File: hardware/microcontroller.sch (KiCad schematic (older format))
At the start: 35 parts, among them P2 USB_OTG, P3 ICSP, P4 STATUS 1, P5 STATUS 2, P6 UART, P7 JTAG, SW1 RESET, U4 ATMEGA32U4-AU, X2 16MHz

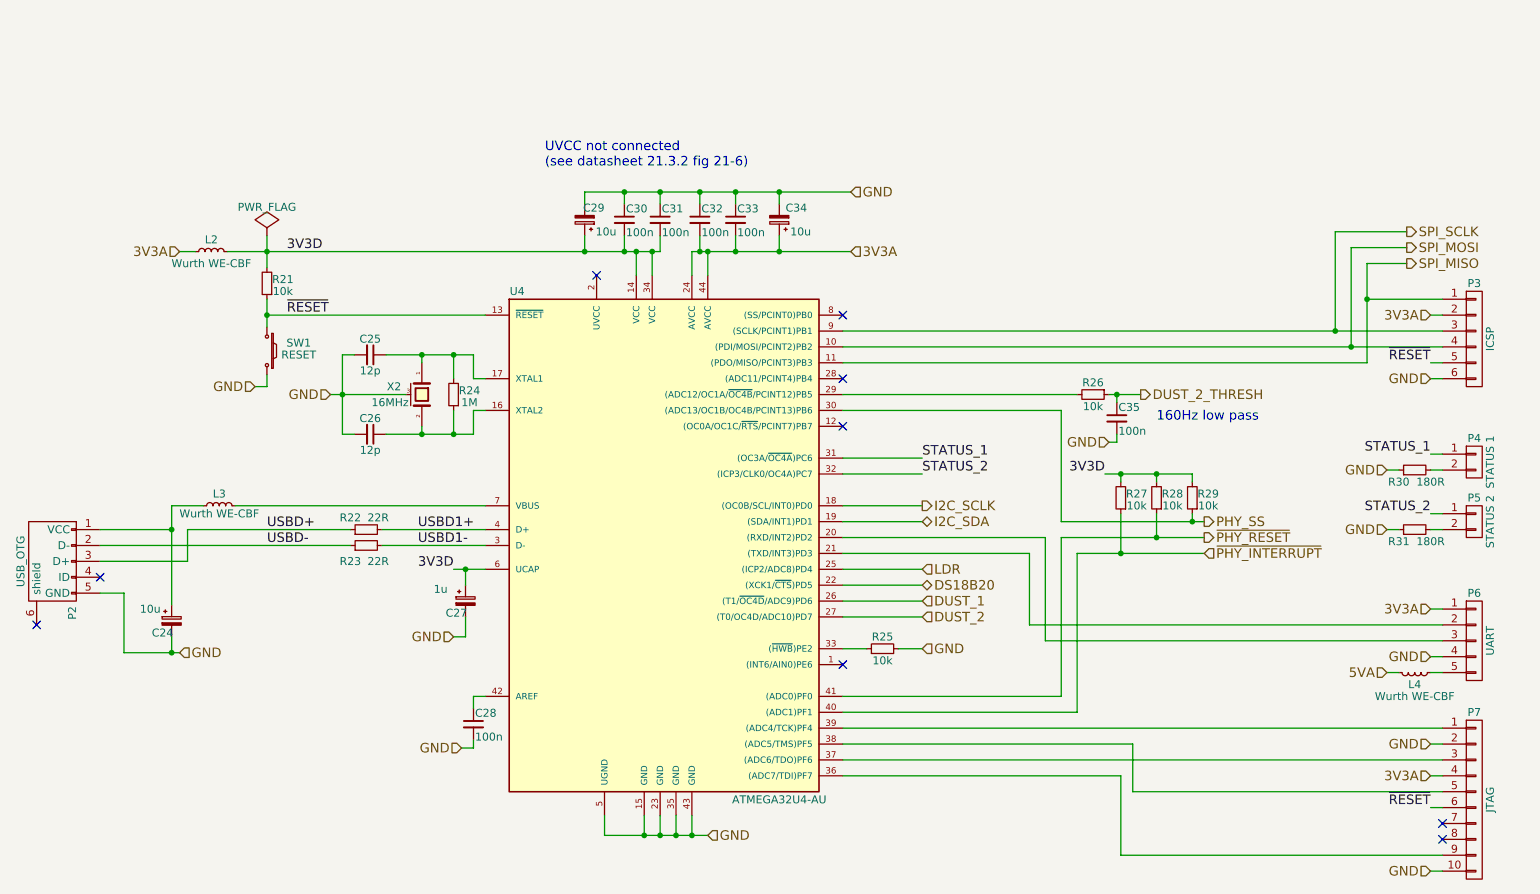
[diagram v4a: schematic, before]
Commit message: Added some part numbers to the schematic
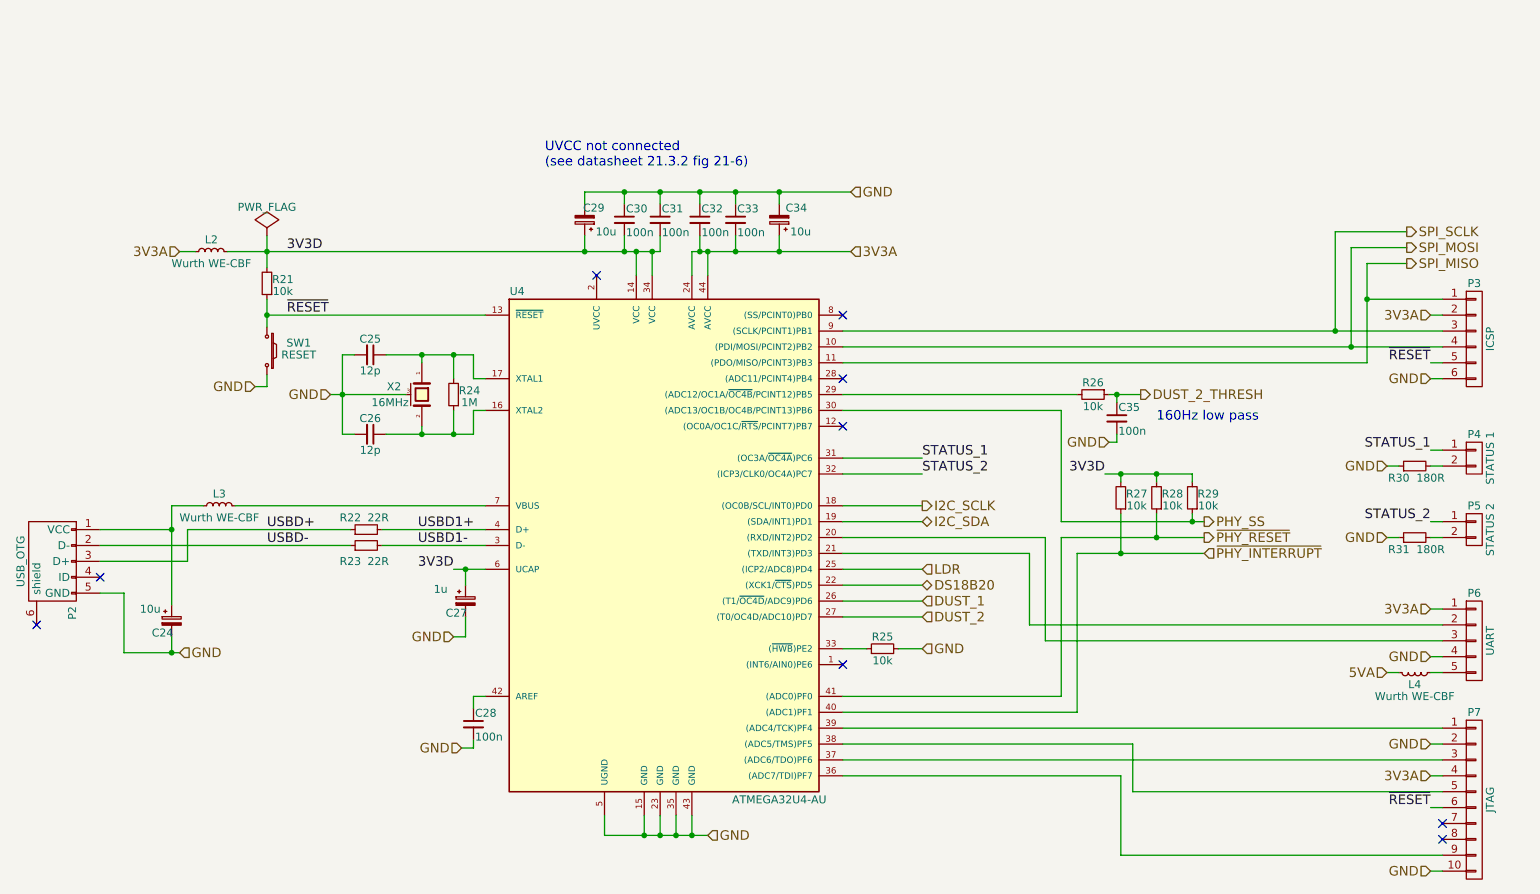
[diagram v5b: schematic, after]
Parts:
- L2, L3, L4: MPN1 (none) -> 7447918; Manufacturer1 (none) -> Wurth Elektronik; SKU1 (none) -> 124-1871; Vendor1 (none) -> RS
- P2: MPN1 (none) -> 10103594-0001LF; Manufacturer1 (none) -> Amphenol; SKU1 (none) -> 649-10103594-0001LF; Vendor1 (none) -> Mouser
- P4, P5: MPN1 (none) -> 22-27-2021; Manufacturer1 (none) -> Molex; SKU1 (none) -> 483-8461; Vendor1 (none) -> RS
- U4: MPN1 (none) -> ATMEGA32U4-AU; Manufacturer1 (none) -> Microchip Technology; SKU1 (none) -> 131-0289; Vendor1 (none) -> RS
- X2: MPN1 (none) -> Q22FA2380018111; Manufacturer1 (none) -> Epson; SKU1 (none) -> 667-6209; Vendor1 (none) -> RS
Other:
- moved on the sheet: P4, R30, R31
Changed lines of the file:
@@
 F 2 "Housings_QFP:TQFP-44_10x10mm_Pitch0.8mm" H 5275 3950 50  0001 C CIN
 F 3 "" H 6375 5050 50  0000 C CNN
+F 4 "Microchip Technology" H 5275 3950 60  0001 C CNN "Manufacturer1"
+F 5 "ATMEGA32U4-AU" H 5275 3950 60  0001 C CNN "MPN1"
+F 6 "RS" H 5275 3950 60  0001 C CNN "Vendor1"
+F 7 "131-0289" H 5275 3950 60  0001 C CNN "SKU1"
 	1    5275 3950
 	1    0    0    -1
@@
 F 2 "Crystals:crystal_FA238-TSX3225" H 3725 2900 50  0001 C CNN
 F 3 "" H 3725 2900 50  0000 C CNN
+F 4 "Epson" V 3725 2900 60  0001 C CNN "Manufacturer1"
+F 5 "Q22FA2380018111" V 3725 2900 60  0001 C CNN "MPN1"
+F 6 "RS" V 3725 2900 60  0001 C CNN "Vendor1"
+F 7 "667-6209" V 3725 2900 60  0001 C CNN "SKU1"
 	1    3725 2900
 	0    1    1    0
@@
 F 2 "Connect:USB_Micro-B_10103594-0001LF" V 1350 3850 50  0001 C CNN
 F 3 "" V 1350 3850 50  0000 C CNN
+F 4 "Amphenol" H 1400 3950 60  0001 C CNN "Manufacturer1"
+F 5 "10103594-0001LF" H 1400 3950 60  0001 C CNN "MPN1"
+F 6 "Mouser" H 1400 3950 60  0001 C CNN "Vendor1"
+F 7 "649-10103594-0001LF" H 1400 3950 60  0001 C CNN "SKU1"
 	1    1400 3950
 	0    -1   1    0
@@
 F 2 "Choke_SMD:Choke_SMD_1206_Standard" H 9975 4650 50  0001 C CNN
 F 3 "" H 9975 4650 50  0000 C CNN
+F 4 "Wurth Elektronik" V 9975 4650 60  0001 C CNN "Manufacturer1"
+F 5 "7447918" V 9975 4650 60  0001 C CNN "MPN1"
+F 6 "RS" V 9975 4650 60  0001 C CNN "Vendor1"
+F 7 "124-1871" V 9975 4650 60  0001 C CNN "SKU1"
 	1    9975 4650
 	0    1    1    0
@@
 $EndComp
 $Comp
-L L_Small L3
-U 1 1 59EF73D9
-P 2450 3600
-F 0 "L3" V 2525 3600 50  0000 C CNN
-F 1 "Wurth WE-CBF" V 2400 3600 50  0000 C CNN
-F 2 "Choke_SMD:Choke_SMD_1206_Standard" H 2450 3600 50  0001 C CNN
-F 3 "" H 2450 3600 50  0000 C CNN
-	1    2450 3600
-	0    -1   -1   0
-$EndComp
-$Comp
 L R_Small R30
 U 1 1 59EFC538
-P 9975 3375
-F 0 "R30" V 9900 3475 50  0000 C CNN
-F 1 "180R" V 9900 3275 50  0000 C CNN
-F 2 "Resistors_SMD:R_1206" H 9975 3375 50  0001 C CNN
-F 3 "" H 9975 3375 50  0000 C CNN
-	1    9975 3375
+P 9975 3350
+F 0 "R30" V 9900 3450 50  0000 C CNN
+F 1 "180R" V 9900 3250 50  0000 C CNN
+F 2 "Resistors_SMD:R_1206" H 9975 3350 50  0001 C CNN
+F 3 "" H 9975 3350 50  0000 C CNN
+	1    9975 3350
 	0    -1   -1   0
 $EndComp
@@
 F 2 "Choke_SMD:Choke_SMD_1206_Standard" H 2400 2000 50  0001 C CNN
 F 3 "" H 2400 2000 50  0000 C CNN
+F 4 "Wurth Elektronik" V 2400 2000 60  0001 C CNN "Manufacturer1"
+F 5 "7447918" V 2400 2000 60  0001 C CNN "MPN1"
+F 6 "RS" V 2400 2000 60  0001 C CNN "Vendor1"
+F 7 "124-1871" V 2400 2000 60  0001 C CNN "SKU1"
 	1    2400 2000
 	0    -1   -1   0
@@
 L CONN_01X02 P4
 U 1 1 59DC89D9
-P 10350 3325
-F 0 "P4" H 10350 3475 50  0000 C CNN
-F 1 "STATUS 1" V 10450 3325 50  0000 C CNN
-F 2 "Connectors_Molex:Molex_KK-6410-02_02x2.54mm_Straight" H 10350 3325 50  0001 C CNN
-F 3 "" H 10350 3325 50  0000 C CNN
-	1    10350 3325
-	1    0    0    -1
-$EndComp
-$Comp
-L CONN_01X02 P5
-U 1 1 59DCC0CC
-P 10350 3700
-F 0 "P5" H 10350 3850 50  0000 C CNN
-F 1 "STATUS 2" V 10450 3700 50  0000 C CNN
-F 2 "Connectors_Molex:Molex_KK-6410-02_02x2.54mm_Straight" H 10350 3700 50  0001 C CNN
-F 3 "" H 10350 3700 50  0000 C CNN
-	1    10350 3700
-	1    0    0    -1
-$EndComp
-Text HLabel 9800 3375 0    60   Input ~ 0
-GND
-Text HLabel 9800 3750 0    60   Input ~ 0
+P 10350 3300
+F 0 "P4" H 10350 3450 50  0000 C CNN
+F 1 "STATUS 1" V 10450 3300 50  0000 C CNN
+F 2 "Connectors_Molex:Molex_KK-6410-02_02x2.54mm_Straight" H 10350 3300 50  0001 C CNN
+F 3 "" H 10350 3300 50  0000 C CNN
+F 4 "Molex" H 10350 3300 60  0001 C CNN "Manufacturer1"
+F 5 "22-27-2021" H 10350 3300 60  0001 C CNN "MPN1"
+F 6 "RS" H 10350 3300 60  0001 C CNN "Vendor1"
+F 7 "483-8461" H 10350 3300 60  0001 C CNN "SKU1"
+	1    10350 3300
+	1    0    0    -1
+$EndComp
+Text HLabel 9800 3350 0    60   Input ~ 0
+GND
+Text HLabel 9800 3800 0    60   Input ~ 0
 GND
 $Comp
 L R_Small R31
 U 1 1 59DCE73D
-P 9975 3750
-F 0 "R31" V 9900 3850 50  0000 C CNN
-F 1 "180R" V 9900 3650 50  0000 C CNN
-F 2 "Resistors_SMD:R_1206" H 9975 3750 50  0001 C CNN
-F 3 "" H 9975 3750 50  0000 C CNN
-	1    9975 3750
+P 9975 3800
+F 0 "R31" V 9900 3900 50  0000 C CNN
+F 1 "180R" V 9900 3700 50  0000 C CNN
+F 2 "Resistors_SMD:R_1206" H 9975 3800 50  0001 C CNN
+F 3 "" H 9975 3800 50  0000 C CNN
+	1    9975 3800
 	0    -1   -1   0
 $EndComp
@@
 Text Label 6875 3400 0    60   ~ 0
 STATUS_2
-Text Label 10075 3275 2    60   ~ 0
+Text Label 10075 3250 2    60   ~ 0
 STATUS_1
-Text Label 10075 3650 2    60   ~ 0
+Text Label 10075 3700 2    60   ~ 0
 STATUS_2
 Text HLabel 6875 4100 2    60   BiDi ~ 0
@@
 	3225 3150 3300 3150
 Wire Wire Line
-	3225 2650 3225 3150
+	3225 2650 3225 2900
+Wire Wire Line
+	3225 2900 3225 3150
 Wire Wire Line
 	3225 2650 3300 2650
 Wire Wire Line
-	3150 2900 3625 2900
+	3150 2900 3225 2900
+Wire Wire Line
+	3225 2900 3625 2900
 Connection ~ 3225 2900
 Wire Wire Line
-	6375 2500 10150 2500
-Wire Wire Line
-	6375 2600 10150 2600
+	6375 2500 9475 2500
+Wire Wire Line
+	9475 2500 10150 2500
+Wire Wire Line
+	6375 2600 9575 2600
+Wire Wire Line
+	9575 2600 10150 2600
 Wire Wire Line
 	9675 2700 6375 2700
 Wire Wire Line
-	2750 2300 2750 2475
+	2750 2300 2750 2400
+Wire Wire Line
+	2750 2400 2750 2475
 Connection ~ 2750 2400
 Wire Wire Line
-	2750 1900 2750 2100
-Wire Wire Line
-	2500 2000 5225 2000
+	2750 1900 2750 2000
+Wire Wire Line
+	2750 2000 2750 2100
+Wire Wire Line
+	2500 2000 2750 2000
+Wire Wire Line
+	2750 2000 4750 2000
+Wire Wire Line
+	4750 2000 5000 2000
+Wire Wire Line
+	5000 2000 5075 2000
+Wire Wire Line
+	5075 2000 5175 2000
+Wire Wire Line
+	5175 2000 5225 2000
 Wire Wire Line
 	10150 2300 9675 2300
 Wire Wire Line
-	9675 2075 9675 2700
+	9675 2075 9675 2300
+Wire Wire Line
+	9675 2300 9675 2700
 Wire Wire Line
 	10075 2400 10150 2400
@@
 	8100 2950 8100 2900
 Wire Wire Line
-	8050 2900 8250 2900
+	8050 2900 8100 2900
+Wire Wire Line
+	8100 2900 8250 2900
 Connection ~ 8100 2900
 Wire Wire Line
@@
 Connection ~ 5075 2000
 Wire Wire Line
-	5425 2000 6425 2000
+	5425 2000 5475 2000
+Wire Wire Line
+	5475 2000 5525 2000
+Wire Wire Line
+	5525 2000 5700 2000
+Wire Wire Line
+	5700 2000 5975 2000
+Wire Wire Line
+	5975 2000 6425 2000
 Wire Wire Line
 	5525 2000 5525 2150
@@
 	4750 1625 4750 1700
 Wire Wire Line
-	4750 1625 6425 1625
+	4750 1625 5000 1625
+Wire Wire Line
+	5000 1625 5225 1625
+Wire Wire Line
+	5225 1625 5475 1625
+Wire Wire Line
+	5475 1625 5700 1625
+Wire Wire Line
+	5700 1625 5975 1625
+Wire Wire Line
+	5975 1625 6425 1625
 Wire Wire Line
 	5000 1625 5000 1700
@@
 Connection ~ 5975 1625
 Wire Wire Line
-	3500 2650 4050 2650
+	3500 2650 3725 2650
+Wire Wire Line
+	3725 2650 3925 2650
+Wire Wire Line
+	3925 2650 4050 2650
 Wire Wire Line
 	3725 2650 3725 2700
 Wire Wire Line
-	3500 3150 4050 3150
+	3500 3150 3725 3150
+Wire Wire Line
+	3725 3150 3925 3150
+Wire Wire Line
+	3925 3150 4050 3150
 Wire Wire Line
 	3725 3150 3725 3100
@@
 	4125 3600 2550 3600
 Wire Wire Line
-	4875 5675 5525 5675
-Wire Wire Line
-	3925 4000 4125 4000
+	4875 5675 5125 5675
+Wire Wire Line
+	5125 5675 5225 5675
+Wire Wire Line
+	5225 5675 5325 5675
+Wire Wire Line
+	5325 5675 5425 5675
+Wire Wire Line
+	5425 5675 5525 5675
+Wire Wire Line
+	3925 4000 4000 4000
+Wire Wire Line
+	4000 4000 4125 4000
 Wire Wire Line
 	4000 4000 4000 4100
@@
 	2350 3600 2150 3600
 Wire Wire Line
-	2150 3600 2150 4225
+	2150 3600 2150 3750
+Wire Wire Line
+	2150 3750 2150 4225
 Wire Wire Line
 	2150 3750 1700 3750
@@
 	1850 4150 1850 4525
 Wire Wire Line
-	1850 4525 2200 4525
+	1850 4525 2150 4525
+Wire Wire Line
+	2150 4525 2200 4525
 Wire Wire Line
 	2150 4525 2150 4425
@@
 	7750 3000 7750 3700
 Wire Wire Line
-	7750 3700 8650 3700
+	7750 3700 8575 3700
+Wire Wire Line
+	8575 3700 8650 3700
 Wire Wire Line
 	8575 3650 8575 3700
@@
 	8575 3400 8575 3450
 Wire Wire Line
-	8025 3400 8575 3400
+	8025 3400 8125 3400
+Wire Wire Line
+	8125 3400 8350 3400
+Wire Wire Line
+	8350 3400 8575 3400
 Wire Wire Line
 	8350 3650 8350 3800
 Wire Wire Line
-	7750 3800 8650 3800
+	7750 3800 8350 3800
+Wire Wire Line
+	8350 3800 8650 3800
 Wire Wire Line
 	8125 3650 8125 3900
 Wire Wire Line
-	7850 3900 8650 3900
+	7850 3900 8125 3900
+Wire Wire Line
+	8125 3900 8650 3900
 Wire Wire Line
 	8350 3450 8350 3400
@@
 	6375 3400 6875 3400
 Wire Wire Line
-	10150 3275 10075 3275
-Wire Wire Line
-	10150 3375 10075 3375
-Wire Wire Line
-	9875 3375 9800 3375
-Wire Wire Line
-	10150 3650 10075 3650
-Wire Wire Line
-	10075 3750 10150 3750
-Wire Wire Line
-	9875 3750 9800 3750
+	10150 3250 10075 3250
+Wire Wire Line
+	10150 3350 10075 3350
+Wire Wire Line
+	9875 3350 9800 3350
+Wire Wire Line
+	10150 3700 10075 3700
+Wire Wire Line
+	10075 3800 10150 3800
+Wire Wire Line
+	9875 3800 9800 3800
 Wire Wire Line
 	6375 4100 6875 4100
+$Comp
+L CONN_01X02 P5
+U 1 1 59DFF1F9
+P 10350 3750
+F 0 "P5" H 10350 3900 50  0000 C CNN
+F 1 "STATUS 2" V 10450 3750 50  0000 C CNN
+F 2 "Connectors_Molex:Molex_KK-6410-02_02x2.54mm_Straight" H 10350 3750 50  0001 C CNN
+F 3 "" H 10350 3750 50  0000 C CNN
+F 4 "Molex" H 10350 3750 60  0001 C CNN "Manufacturer1"
+F 5 "22-27-2021" H 10350 3750 60  0001 C CNN "MPN1"
+F 6 "RS" H 10350 3750 60  0001 C CNN "Vendor1"
+F 7 "483-8461" H 10350 3750 60  0001 C CNN "SKU1"
+	1    10350 3750
+	1    0    0    -1
+$EndComp
+$Comp
+L L_Small L3
+U 1 1 59E04F6E
+P 2450 3600
+F 0 "L3" V 2525 3600 50  0000 C CNN
+F 1 "Wurth WE-CBF" V 2375 3600 50  0000 C CNN
+F 2 "Choke_SMD:Choke_SMD_1206_Standard" H 2450 3600 50  0001 C CNN
+F 3 "" H 2450 3600 50  0000 C CNN
+F 4 "Wurth Elektronik" V 2450 3600 60  0001 C CNN "Manufacturer1"
+F 5 "7447918" V 2450 3600 60  0001 C CNN "MPN1"
+F 6 "RS" V 2450 3600 60  0001 C CNN "Vendor1"
+F 7 "124-1871" V 2450 3600 60  0001 C CNN "SKU1"
+	1    2450 3600
+	0    -1   -1   0
+$EndComp
 $EndSCHEMATC
